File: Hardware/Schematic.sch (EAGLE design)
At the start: 103 parts, among them IC1 XC6220A331MR-G, IC2 BD5229G-TR, J1 SAMACSYS_PARTS_USB4110-GF-A, J2 QWIIC_RIGHT_ANGLE, J3 FH34SRJ-24S-0.5SH_99_, J4 112A-TAAR-R03_ATTENDPACHET, Q1 20V/4.2A/52mΩ/1.4W, Q2 SI1308EDL-T1-GE3, Q3 20V/4.2A/52mΩ/1.4W, U1 ESP32-C6-WROOM-1-N8, U2 MAX17048G+T10, U3 W25Q512JVEIQ, U4 DS3231SN#

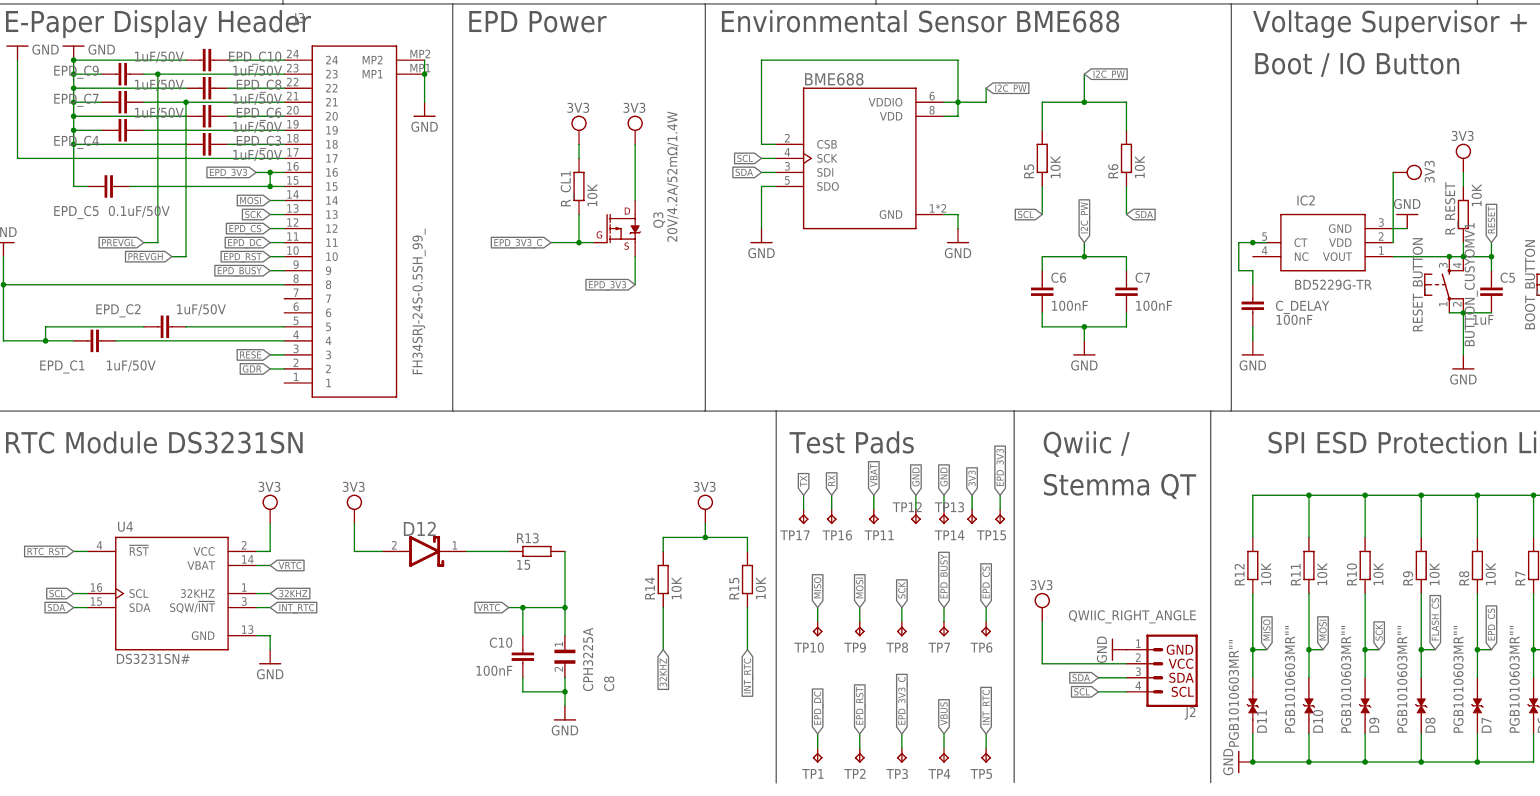
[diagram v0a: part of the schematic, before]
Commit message: Fixes #1. #2. #3. #4. #5. #6. #7 #8 #9: Improved 3D models, silkscreen and schematic
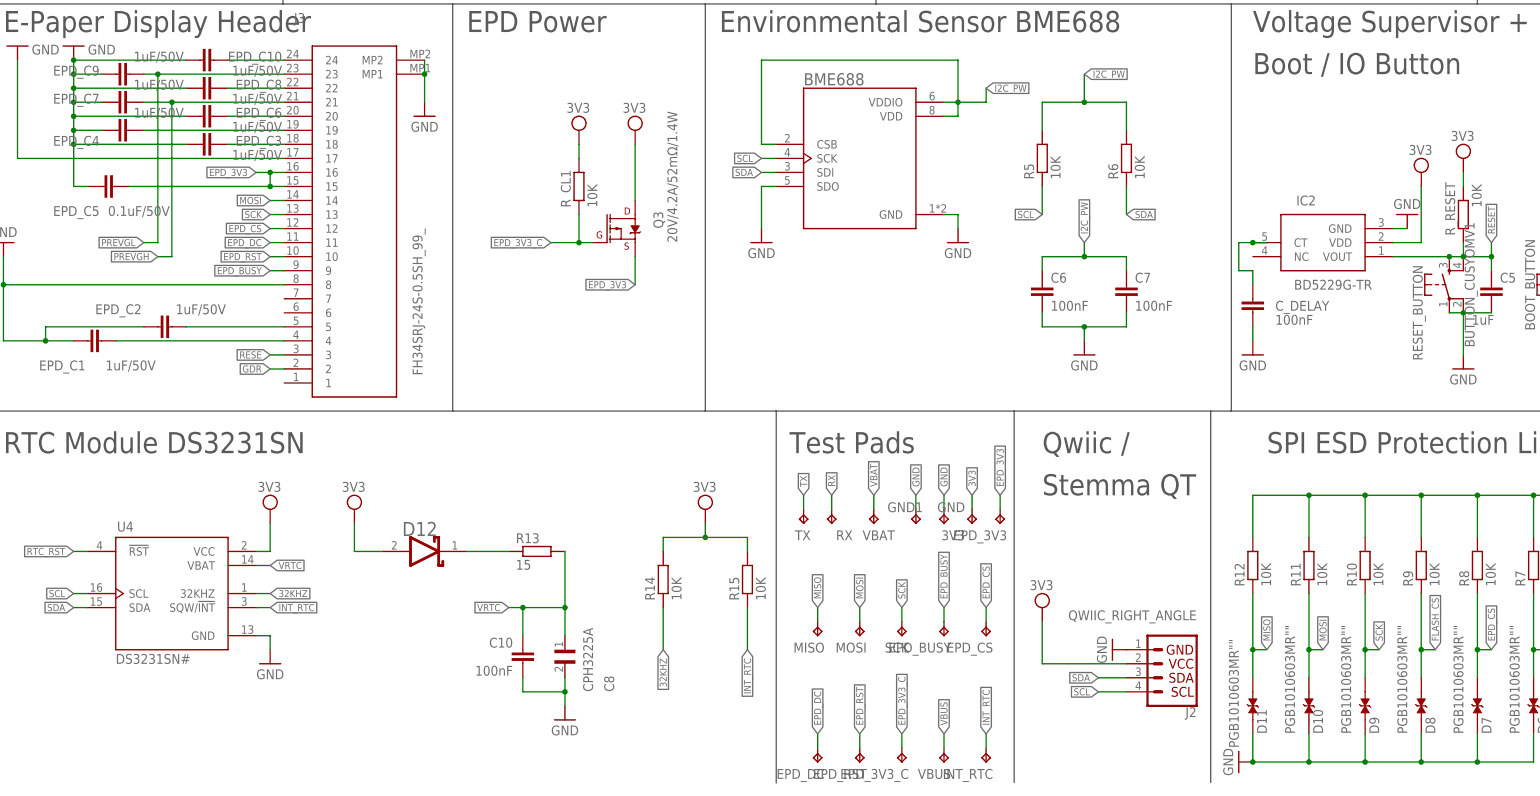
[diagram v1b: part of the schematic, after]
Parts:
- renumbered TP1 to EPD_DC, TP10 to MISO, TP11 to VBAT, TP12 to GND1, TP13 to GND, TP14 to 3V3, TP15 to EPD_3V3, TP16 to RX, TP17 to TX, TP2 to EPD_RST, TP3 to EPD_3V3_C, TP4 to VBUS, TP5 to INT_RTC, TP6 to EPD_CS, TP7 to EPD_BUSY, TP8 to SCK, TP9 to MOSI
